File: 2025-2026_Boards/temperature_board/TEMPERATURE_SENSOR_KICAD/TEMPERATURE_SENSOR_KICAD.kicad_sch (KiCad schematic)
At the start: 55 parts, among them J1 LCD Connector Pinout, U1 STM32G431CBT6, U2 TMP235A4DBZR, U3 AMS1117-3.3, U5 TPS62932DRLR, U6 TPS62932DRLR, U8 AMS1117

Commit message: Added test LEDs
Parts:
- added D3: DEBUG LED 1, Capacitor_SMD:C_0201_0603Metric, symbol Device:LED
- added D4: DEBUG LED 2, Capacitor_SMD:C_0201_0603Metric, symbol Device:LED
- added R3, R4: 1k5, Resistor_SMD:R_0402_1005Metric, symbol Device:R
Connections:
- net GND: now also R3.2, R4.2
- net at U1.5 (PF0): now also D3.2 (A)
- net at U1.6 (PF1): now also D4.2 (A)
- new net: D4.1 (K), R4.1
- new net: D3.1 (K), R3.1
- no-connect marks 4 -> 23

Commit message: finalizing board
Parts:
- removed Cboot1: 100n, Capacitor_SMD:C_0402_1005Metric, symbol Device:C
- removed Cin1, Cin2: 10u, Capacitor_SMD:C_1210_3225Metric, symbol Device:C
- removed Cinx1, Cinx2: 100n, Capacitor_SMD:C_0603_1608Metric, symbol Device:C
- removed Cout1, Cout2: 47u, Capacitor_SMD:C_1210_3225Metric, symbol Device:C
- removed Css1: 33n, Capacitor_SMD:C_01005_0402Metric, symbol Device:C
- removed L3: 22u, Inductor_THT:L_Radial_D13.5mm_P7.00mm_Fastron_09HCP, symbol Device:L
- removed Rfbb1: 10k, Resistor_SMD:R_0402_1005Metric, symbol Device:R
- removed Rfbt1: 140k, Resistor_SMD:R_0201_0603Metric, symbol Device:R
- removed TP2: TestPoint, Connector_Pin:Pin_D1.3mm_L10.0mm_W3.5mm_Flat, symbol Connector:TestPoint
- removed U6: TPS62932DRLR, AdditionalFootprintLibrary:SOT8_DRL_TEX-M, symbol 2025-10-19_16-52-39:TPS62932DRLR
- added Cen2: 10n, Capacitor_SMD:C_0201_0603Metric, symbol Device:C
- added Cin3: 10u, Capacitor_SMD:C_0201_0603Metric, symbol Device:C
- added Cin4: 10u, Capacitor_SMD:C_1210_3225Metric, symbol Device:C
- added Cinx3: 100n, Capacitor_SMD:C_0201_0603Metric, symbol Device:C
- added Cinx4: 100n, Capacitor_SMD:C_0603_1608Metric, symbol Device:C
- added Cout4: 47u, Capacitor_SMD:C_1210_3225Metric, symbol Device:C
- added Renb2, Rent2: 10k, Resistor_SMD:R_0201_0603Metric, symbol Device:R
- added VR2: TPSM863252RDXR, AdditionalFootprintLibrary:VREG_TPSM863252RDXR, symbol TPSM863252RDXR:TPSM863252RDXR
- added cff1, cout3: 22p, Capacitor_SMD:C_0201_0603Metric, symbol Device:C
- added rfbb2: 30k, Resistor_SMD:R_0201_0603Metric, symbol Device:R
- added rfbt2: 80.6k, Resistor_SMD:R_0201_0603Metric, symbol Device:R
- renumbered Rfbb2 to Rfbb1, Rfbt2 to Rfbt1
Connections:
- net +2.2V: now also VR2.3 (VOUT), cff1.1, cout3.1, rfbt2.1
- net +3.3V: now also Cin3.1, Cinx3.1, Rent2.1, VR2.1 (VIN)
- net 28V: now also Cin4.1, Cinx4.1
- net 5V: now also Cout4.1
- net GND: now also Cen2.2, Cin3.2, Cin4.2, Cinx3.2, Cinx4.2, Cout4.2, Renb2.2, VR2.4 (PGND), cout3.2, rfbb2.2
- new net: Cen2.1, Renb2.1, Rent2.2, VR2.6 (EN)
- new net: VR2.7 (FB), cff1.2, rfbb2.1, rfbt2.2
- no-connect marks 23 -> 20
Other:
- note removed: "BUCK CONVERTER (28V TO 12V, 2A)"
- moved on the sheet: C1, C10, C11, C12, C13, C14, C2, C24, C25, C3, C4, C5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

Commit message: Finalizations
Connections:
- no-connect marks 20 -> 22
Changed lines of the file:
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@@
+	)
+	(no_connect
+		(at 60.96 102.87)
 	)
 	(no_connect
@@
 	)
 	(no_connect
+		(at 60.96 100.33)
+	)
+	(no_connect

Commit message: updates
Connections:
- net FDCAN_RX renamed FDCAN_-
- net FDCAN_TX renamed FDCAN_+
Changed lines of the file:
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@@
 		)
 	)
-	(global_label "FDCAN_TX"
+	(global_label "FDCAN_+"
 		(shape input)
 		(at 93.98 113.03 0)
@@
 		)
 		(property "Intersheetrefs" "${INTERSHEET_REFS}"
-			(at 106.1576 113.03 0)
+			(at 105.5529 113.03 0)
 			(effects
 				(font
@@
 		)
 	)
-	(global_label "FDCAN_RX"
+	(global_label "FDCAN_-"
 		(shape input)
 		(at 93.98 110.49 0)
@@
 		)
 		(property "Intersheetrefs" "${INTERSHEET_REFS}"
-			(at 106.46 110.49 0)
+			(at 105.5529 110.49 0)
 			(effects
 				(font

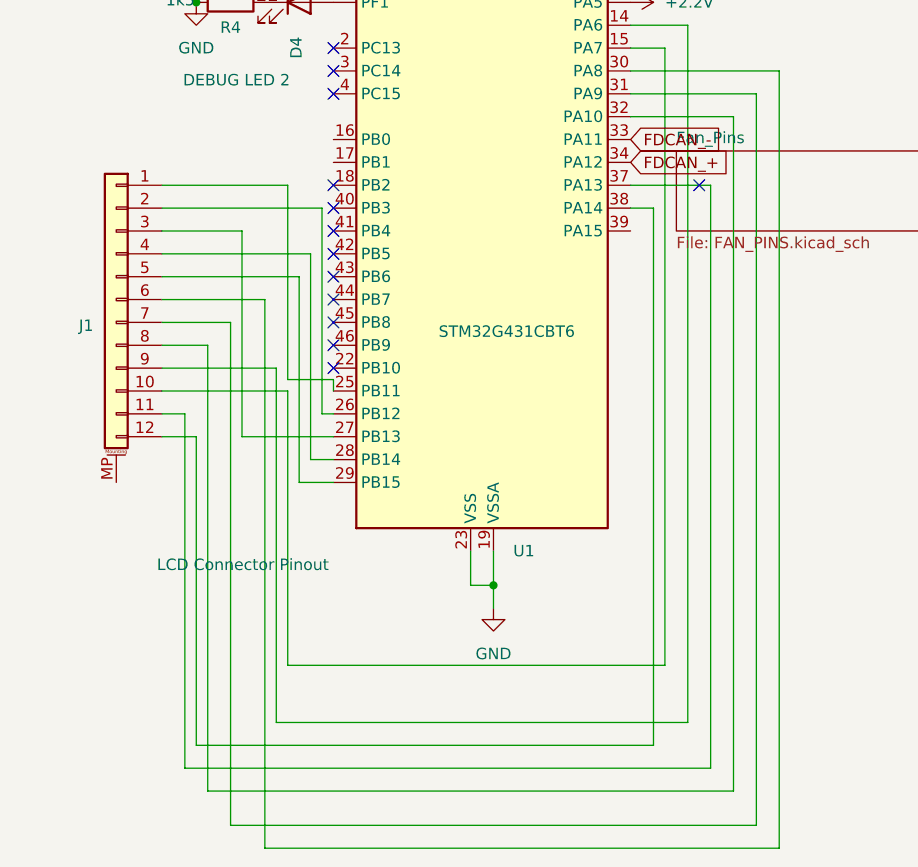
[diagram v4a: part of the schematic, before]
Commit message: fixed differential pair and made new lcd wiring
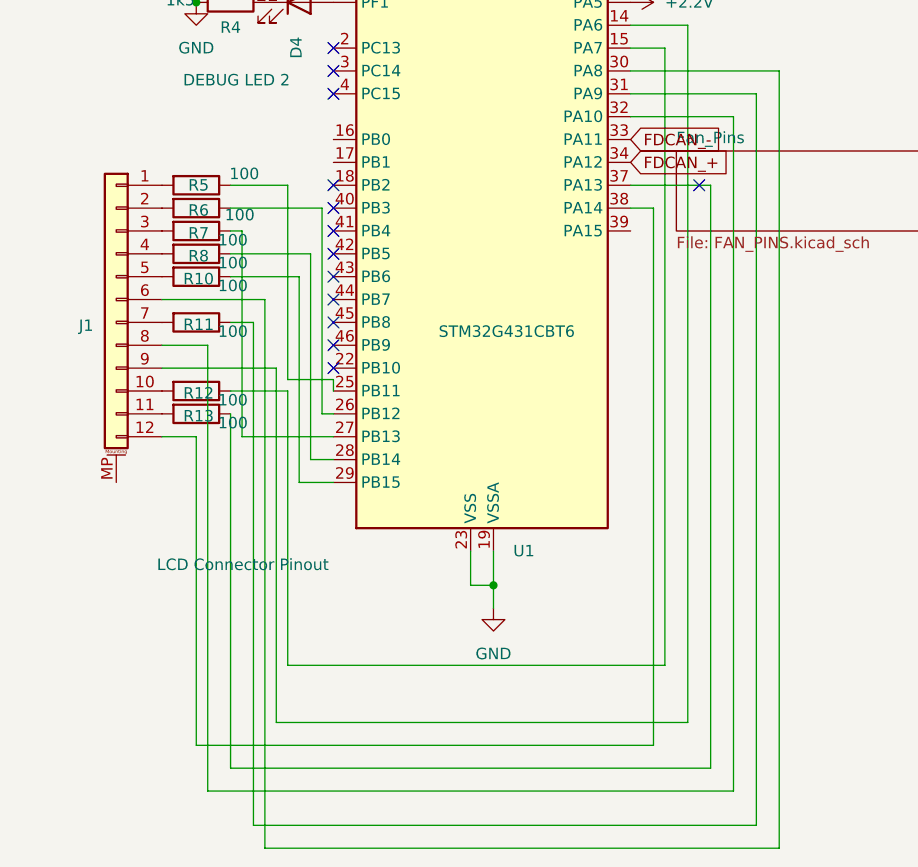
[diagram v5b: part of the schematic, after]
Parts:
- added R10, R11, R12, R13, R5, R6, R7, R8: 100, Resistor_SMD:R_0201_0603Metric, symbol Device:R
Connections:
- net at U1.15 (PA7): now also R12.1; no longer J1.10 (Pin_10)
- net at U1.25 (PB11): now also R5.1; no longer J1.1 (Pin_1)
- net at U1.26 (PB12): now also R6.1; no longer J1.2 (Pin_2)
- net at U1.27 (PB13): now also R7.1; no longer J1.3 (Pin_3)
- net at U1.28 (PB14): now also R8.1; no longer J1.4 (Pin_4)
- net at U1.29 (PB15): now also R10.1; no longer J1.5 (Pin_5)
- net at U1.31 (PA9): now also R11.1; no longer J1.7 (Pin_7)
- net at U1.37 (PA13): now also R13.1; no longer J1.11 (Pin_11)
- new net: J1.5 (Pin_5), R10.2
- new net: J1.2 (Pin_2), R6.2
- new net: J1.1 (Pin_1), R5.2
- new net: J1.7 (Pin_7), R11.2
- new net: J1.10 (Pin_10), R12.2
- new net: J1.11 (Pin_11), R13.2
- new net: J1.3 (Pin_3), R7.2
- new net: J1.4 (Pin_4), R8.2
